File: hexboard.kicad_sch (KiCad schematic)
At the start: 34 parts, among them J1 USB_C_Receptacle_USB2.0_16P, J2 USB_A, J3 Conn_01x20, J4 Conn_01x20, SW1 SW_Push, SW2 SW_Push, U1 RP2040, U2 MCP1700x-330xxTT, U3 W25Q16JVSS, Y1 Crystal_GND23_Small

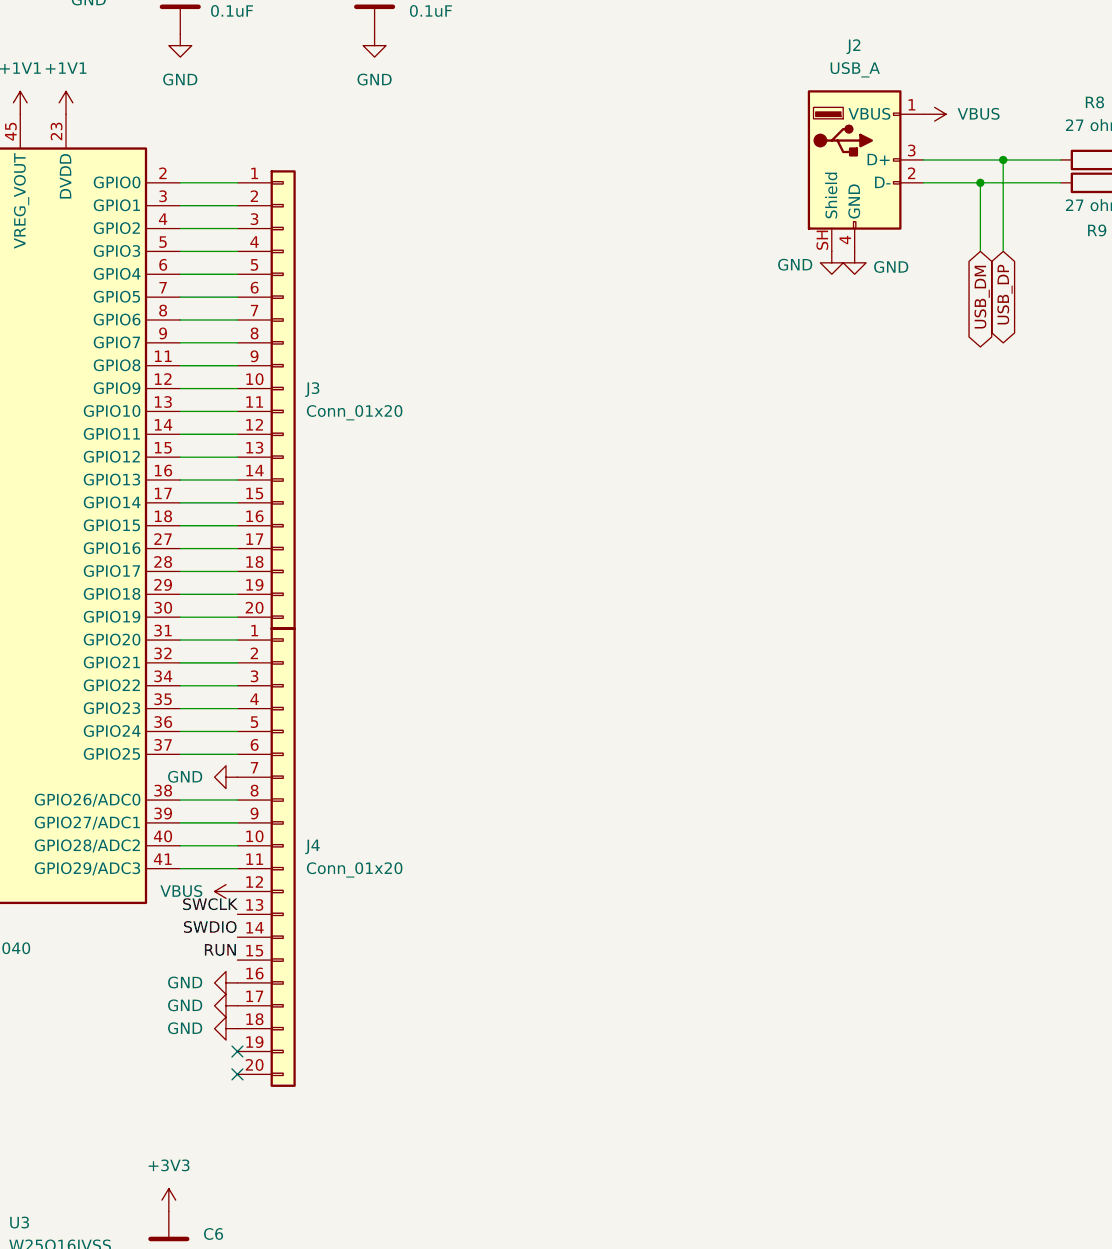
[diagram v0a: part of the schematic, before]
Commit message: added hexagon design and handle on the front and started adding an oled header
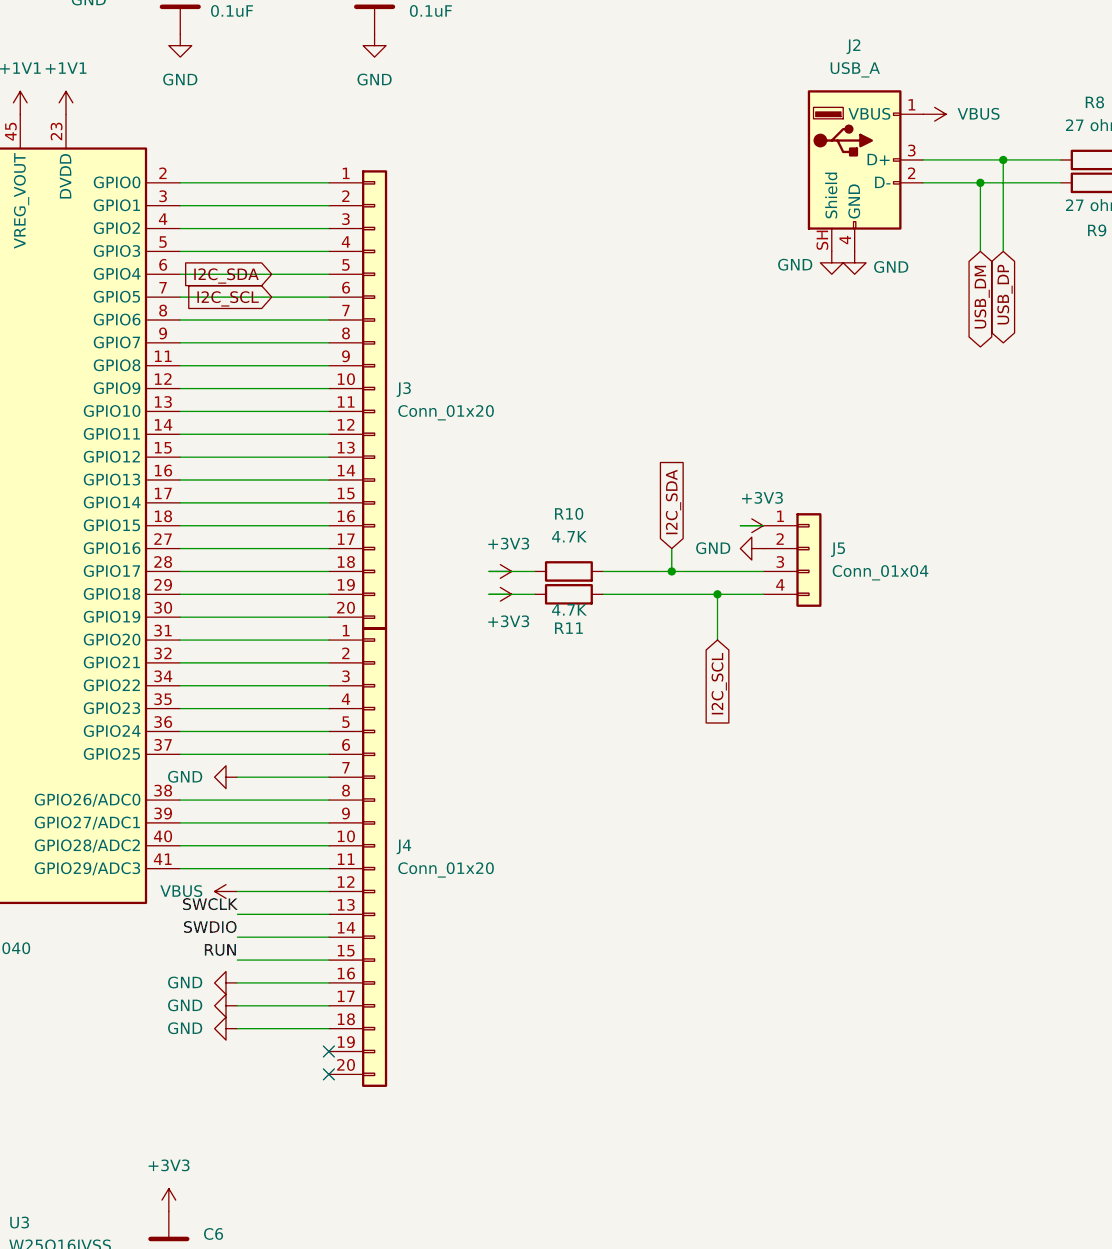
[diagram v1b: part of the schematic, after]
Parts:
- added J5: Conn_01x04, symbol Connector_Generic:Conn_01x04
- added R10: 4.7K, Connector_PinHeader_2.54mm:PinHeader_1x04_P2.54mm_Vertical, symbol Device:R
- added R11: 4.7K, Resistor_SMD:R_0402_1005Metric, symbol Device:R
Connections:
- net +3V3: now also J5.1 (Pin_1), R10.1, R11.1
- net GND: now also J5.2 (Pin_2)
- net I2C_SDA: now reaches J3.5 (Pin_5), U1.6 (GPIO4)
- net I2C_SDA: now also J5.3 (Pin_3), R10.2
- net I2C_SCL: now reaches J3.6 (Pin_6), U1.7 (GPIO5)
- net I2C_SCL: now also J5.4 (Pin_4), R11.2
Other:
- moved on the sheet: J3, J4
